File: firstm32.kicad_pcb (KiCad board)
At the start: 2 copper layers, 36 parts, among them J1 USB_C_Receptacle_USB2.0_16P, J2 Conn_01x04_Pin, J3 Conn_01x04_Pin, J4 Conn_01x04_Pin, SW1 SW_SPDT, U1 AMS1117-3.3, U2 STM32F103C8T6, Y1 16MHz

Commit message: Finished board layout
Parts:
- added H1: MountingHole, MountingHole:MountingHole_2.2mm_M2, F.Cu at (128.5, 91.5)
- added H2: MountingHole, MountingHole:MountingHole_2.2mm_M2, F.Cu at (167.5, 91.5)
- added H3: MountingHole, MountingHole:MountingHole_2.2mm_M2, F.Cu at (167.5, 118.5)
- added H4: MountingHole, MountingHole:MountingHole_2.2mm_M2, F.Cu at (128.5, 118.5)
- moved TP4 65.7 mm to (162.0, 95.8)
- moved R1 56.5 mm to (135.5, 99.0)
- moved D2 51.8 mm to (130.0, 113.0), turned to 90 degrees
- moved D1 47.6 mm to (133.0, 113.0), turned to 90 degrees
- moved C6 45.9 mm to (142.8, 107.0), turned to -90 degrees
- moved C9 44.9 mm to (144.5, 110.0), turned to -90 degrees
- moved J3 42.8 mm to (142.5, 91.0)
- moved R4 42.3 mm to (157.5, 103.1), turned to 90 degrees
- moved TP3 41.7 mm to (152.5, 114.2)
- moved R3 41.0 mm to (160.2, 103.0)
- moved J2 40.8 mm to (154.5, 91.0)
- moved TP1 39.1 mm to (133.0, 105.9)
- moved U1 38.1 mm to (157.8, 114.8), turned to -90 degrees
- moved R2 36.5 mm to (160.2, 105.8)
- moved TP2 35.7 mm to (152.5, 117.5)
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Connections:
- J4 pad 2: /I2C2_SDA -> /I2C2_SCL
- J4 pad 3: /I2C2_SCL -> /I2C2_SDA
- R7 pad 1: /I2C2_SCL -> /I2C2_SDA
- R8 pad 1: /I2C2_SDA -> /I2C2_SCL
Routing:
- net +3V3: track 0.00 -> 136.4 mm, vias 0 -> 7
- net GND: track 0.00 -> 31.1 mm, vias 0 -> 27
- net DEBUG: track 0.00 -> 20.0 mm, vias 0 -> 1
- net /SWDIO: track 0.00 -> 15.2 mm
- net /I2C2_SCL: track 0.00 -> 14.5 mm
- net /BOOT0: track 0.00 -> 13.9 mm
- net /I2C2_SDA: track 0.00 -> 13.3 mm
- net /USB_D+: track 0.00 -> 12.8 mm
- net /USART_RX: track 0.00 -> 12.7 mm
- net /USART_TX: track 0.00 -> 11.9 mm
- net /USB_D-: track 0.00 -> 11.3 mm
- net /SWCLK: track 0.00 -> 10.7 mm
- net VBUS: track 0.00 -> 10.6 mm, vias 0 -> 2
- net /HSE_IN: track 0.00 -> 7.21 mm
- net /NRST: track 0.00 -> 5.89 mm
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- added copper zone on F.Cu, net +3V3
- added copper zone on B.Cu, net GND
- added copper zone on F.Cu, net GND
- added copper zone on F.Cu, net VBUS
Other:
- board outline added: 44 x 32 mm
- board text added: "3V3"
- board text added: "DEBUG"
- board text added: "GND"
- board text added: "LDO"
- board text added: "PWR"
- board text added: "VBUS"

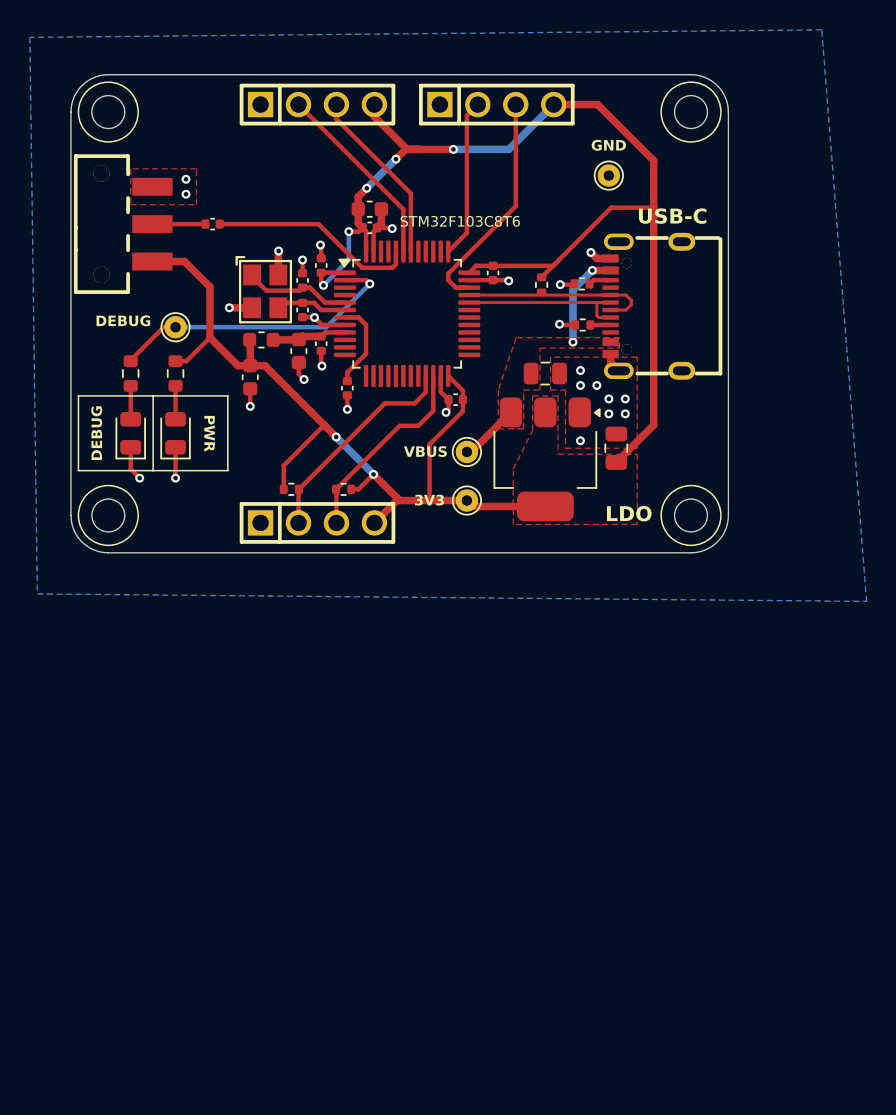
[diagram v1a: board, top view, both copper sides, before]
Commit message: Finalised board and ordered with JLCPCC + PCBA
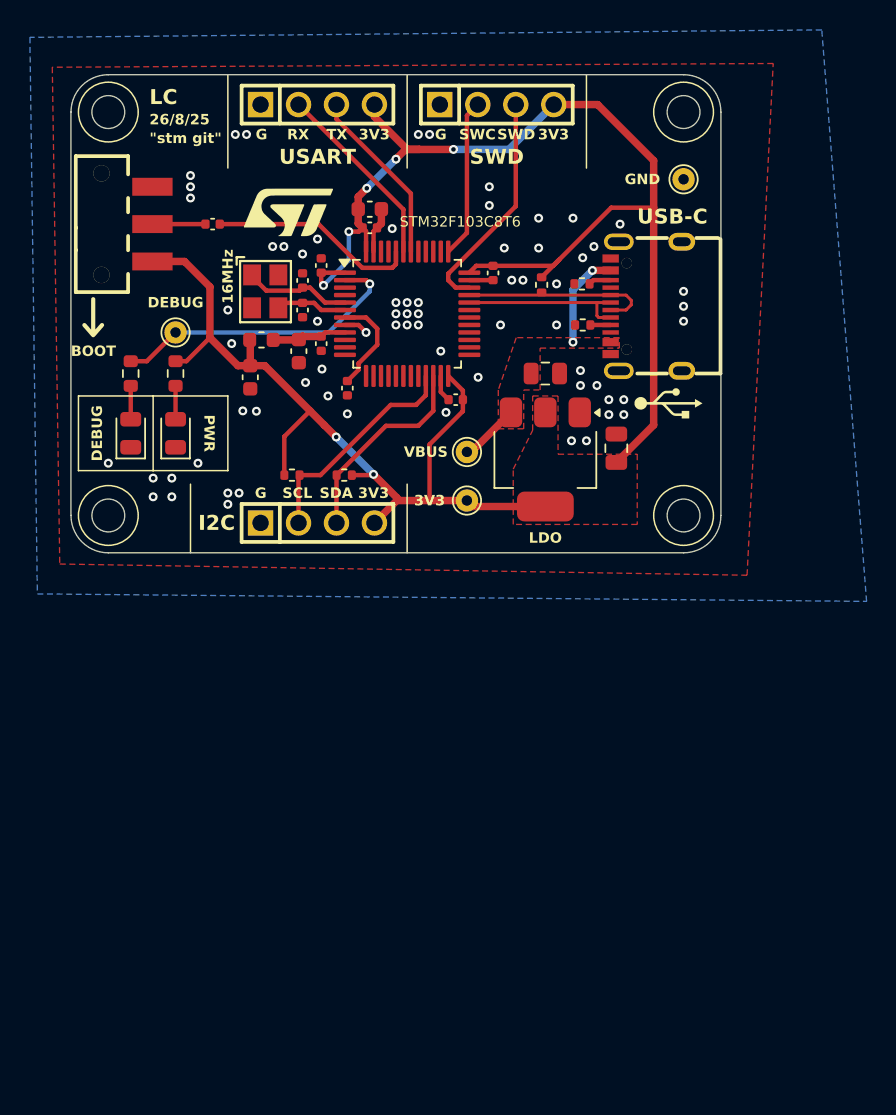
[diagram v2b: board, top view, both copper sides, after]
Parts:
- added G***: LOGO, LOGO, F.Cu at (140.5, 98.2)
- added G***: LOGO, LOGO, F.Cu at (127.5, 105.2)
- added G***: LOGO, LOGO, F.Cu at (166.0, 111.0)
- moved TP4 5.01 mm to (167.0, 96.0)
- moved R7 0.95 mm to (144.3, 115.8)
- moved R8 0.95 mm to (140.8, 115.8)
- moved H2 0.50 mm to (167.0, 91.5)
- moved H3 0.50 mm to (167.0, 118.5)
- moved TP1 0.35 mm to (133.0, 106.2)
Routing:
- net GND: track 31.1 -> 8.21 mm, vias 27 -> 69
- net /NRST: track 5.89 -> 6.80 mm
- net +3V3: track 136.4 -> 135.5 mm
- net /I2C2_SCL: track 14.5 -> 15.2 mm
- net /I2C2_SDA: track 13.3 -> 13.8 mm
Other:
- board size 44 x 32 mm -> 43.5 x 32 mm
- board text added: "16MHz"
- board text added: "26/8/25"
- board text added: "BOOT"
- board text added: "G"
- board text added: "I2C"
- board text added: "JLCJLCJLCJLC"
- board text added: "LC"
- board text added: "RX"
- board text added: "SCL"
- board text added: "SDA"
- board text added: "SWC"
- board text added: "SWD"
- board text added: "TX"
- board text added: "USART"
- board text added: "{dblquote}stm git{dblquote}"
